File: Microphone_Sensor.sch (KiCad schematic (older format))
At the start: 21 parts

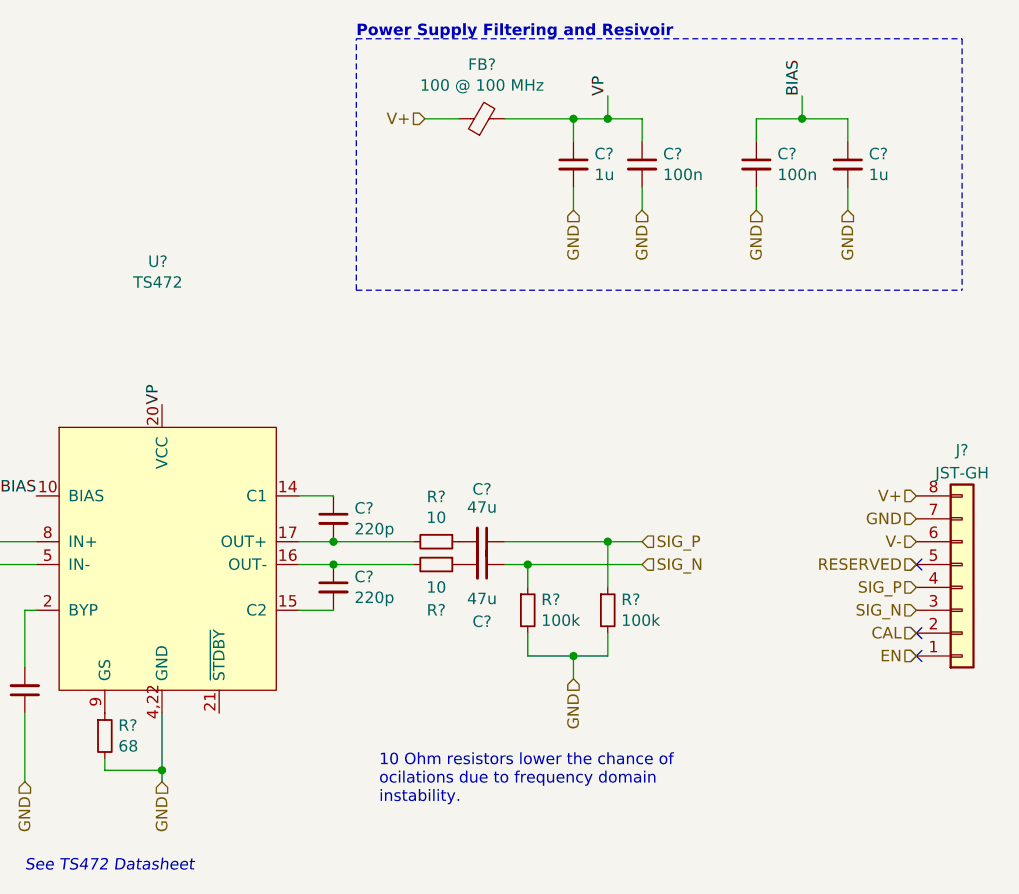
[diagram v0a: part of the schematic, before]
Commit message: Change Connector Layout
Also add Mic. board to connectors
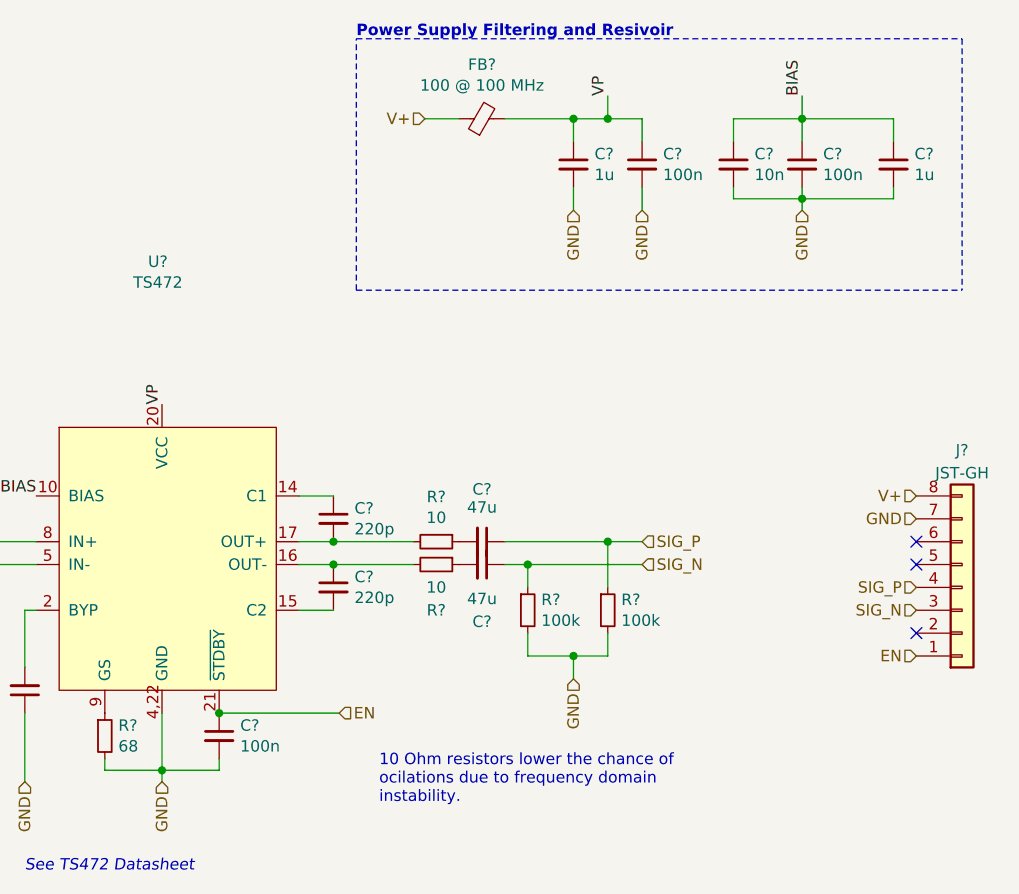
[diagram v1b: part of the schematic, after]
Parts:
- added C?: 100n, symbol Device:C_Small
- added C?: 10n, symbol Device:C_Small
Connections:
- net BIAS: now also C?.1
- net EN: now also U?.21 (~STDBY), C?.1
- net GND: now also C?.2, C?.2
- net CAL: no longer names the net of J?.2 (Pin_2)
- net RESERVED: no longer names the net of J?.5 (Pin_5)
- net V-: no longer names the net of J?.6 (Pin_6)
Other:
- moved on the sheet: C?
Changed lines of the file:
@@
 $Descr A4 11693 8268
 encoding utf-8
-Sheet 14 14
+Sheet 12 14
 Title ""
 Date ""
@@
 U 1 1 5EEDE2AE
 P 4150 2900
+AR Path="/5EE5ECAD/5EECE6B8/5EEDE2AE" Ref="MK?"  Part="1"
+AR Path="/5EE5ECAD/5EF21991/5EEDE2AE" Ref="MK?"  Part="1"
+AR Path="/5EE5ECAD/5EF33EA2/5EEDE2AE" Ref="MK?"  Part="1"
 F 0 "MK?" H 3623 2921 50  0000 R CNN
 F 1 "MIC_ICS_40300" H 3623 2830 50  0000 R CNN
@@
 U 1 1 5EEDEA2B
 P 5150 2900
+AR Path="/5EE5ECAD/5EECE6B8/5EEDEA2B" Ref="C?"  Part="1"
+AR Path="/5EE5ECAD/5EF21991/5EEDEA2B" Ref="C?"  Part="1"
+AR Path="/5EE5ECAD/5EF33EA2/5EEDEA2B" Ref="C?"  Part="1"
 F 0 "C?" V 4921 2900 50  0000 C CNN
 F 1 "1u" V 5000 2900 50  0000 C CNN
@@
 AR Path="/5EE5ECAD/5EE94935/5EEE2D96" Ref="J?"  Part="1"
 AR Path="/5EE1D522/5EEE2D96" Ref="J?"  Part="1"
+AR Path="/5EE5ECAD/5EECE6B8/5EEE2D96" Ref="J?"  Part="1"
+AR Path="/5EE5ECAD/5EF21991/5EEE2D96" Ref="J?"  Part="1"
+AR Path="/5EE5ECAD/5EF33EA2/5EEE2D96" Ref="J?"  Part="1"
 F 0 "J?" H 9950 2500 50  0000 C CNN
 F 1 "JST-GH" H 9950 2600 50  0000 C CNN
@@
 L Device:C_Small C?
 U 1 1 5EEFDD4C
-P 9050 1250
-F 0 "C?" H 9142 1296 50  0000 L CNN
-F 1 "100n" H 9142 1205 50  0000 L CNN
-F 2 "" H 9050 1250 50  0001 C CNN
-F 3 "~" H 9050 1250 50  0001 C CNN
-	1    9050 1250
-	1    0    0    -1
-$EndComp
-Wire Wire Line
-	9050 1050 9050 1150
-Wire Wire Line
-	9050 1350 9050 1450
+P 9250 1250
+AR Path="/5EE5ECAD/5EECE6B8/5EEFDD4C" Ref="C?"  Part="1"
+AR Path="/5EE5ECAD/5EF21991/5EEFDD4C" Ref="C?"  Part="1"
+AR Path="/5EE5ECAD/5EF33EA2/5EEFDD4C" Ref="C?"  Part="1"
+F 0 "C?" H 9342 1296 50  0000 L CNN
+F 1 "100n" H 9342 1205 50  0000 L CNN
+F 2 "" H 9250 1250 50  0001 C CNN
+F 3 "~" H 9250 1250 50  0001 C CNN
+	1    9250 1250
+	1    0    0    -1
+$EndComp
+Wire Wire Line
+	9250 1050 9250 1150
+Wire Wire Line
+	9250 1350 9250 1400
 Text Notes 7300 700  0    50   ~ 10
 Power Supply Filtering and Resivoir
@@
 Text HLabel 9750 2800 0    50   Input ~ 0
 GND
-Text HLabel 9750 2900 0    50   Input ~ 0
-V-
 Text HLabel 9750 3100 0    50   Input ~ 0
 SIG_P
 Text HLabel 9750 3200 0    50   Input ~ 0
 SIG_N
-Text HLabel 9750 3300 0    50   Input ~ 0
-CAL
 Text HLabel 9750 3400 0    50   Input ~ 0
 EN
-Text HLabel 9750 3000 0    50   Input ~ 0
-RESERVED
 NoConn ~ 9750 3000
-NoConn ~ 9750 3400
 NoConn ~ 9750 3300
 $Comp
@@
 U 1 1 5EF35019
 P 7850 1050
+AR Path="/5EE5ECAD/5EECE6B8/5EF35019" Ref="FB?"  Part="1"
+AR Path="/5EE5ECAD/5EF21991/5EF35019" Ref="FB?"  Part="1"
+AR Path="/5EE5ECAD/5EF33EA2/5EF35019" Ref="FB?"  Part="1"
 F 0 "FB?" V 8087 1050 50  0000 C CNN
 F 1 "100 @ 100 MHz" V 7996 1050 50  0000 C CNN
@@
 Text HLabel 7600 1050 0    50   Input ~ 0
 V+
-Text HLabel 9050 1450 3    50   Input ~ 0
+Text HLabel 9250 1450 3    50   Input ~ 0
 GND
 Wire Notes Line
@@
 U 1 1 5EE1252E
 P 6450 2950
+AR Path="/5EE5ECAD/5EECE6B8/5EE1252E" Ref="U?"  Part="1"
+AR Path="/5EE5ECAD/5EF21991/5EE1252E" Ref="U?"  Part="1"
+AR Path="/5EE5ECAD/5EF33EA2/5EE1252E" Ref="U?"  Part="1"
 F 0 "U?" H 6432 4225 50  0000 C CNN
 F 1 "TS472" H 6432 4134 50  0000 C CNN
@@
 U 1 1 5EE150A7
 P 4950 3000
+AR Path="/5EE5ECAD/5EECE6B8/5EE150A7" Ref="R?"  Part="1"
+AR Path="/5EE5ECAD/5EF21991/5EE150A7" Ref="R?"  Part="1"
+AR Path="/5EE5ECAD/5EF33EA2/5EE150A7" Ref="R?"  Part="1"
 F 0 "R?" V 5150 3000 50  0000 C CNN
 F 1 "220" V 5050 3000 50  0000 C CNN
@@
 U 1 1 5EE19951
 P 5150 3000
+AR Path="/5EE5ECAD/5EECE6B8/5EE19951" Ref="C?"  Part="1"
+AR Path="/5EE5ECAD/5EF21991/5EE19951" Ref="C?"  Part="1"
+AR Path="/5EE5ECAD/5EF33EA2/5EE19951" Ref="C?"  Part="1"
 F 0 "C?" V 5400 3000 50  0000 C CNN
 F 1 "1u" V 5300 3000 50  0000 C CNN
@@
 U 1 1 5EE1EACE
 P 5850 3550
+AR Path="/5EE5ECAD/5EECE6B8/5EE1EACE" Ref="C?"  Part="1"
+AR Path="/5EE5ECAD/5EF21991/5EE1EACE" Ref="C?"  Part="1"
+AR Path="/5EE5ECAD/5EF33EA2/5EE1EACE" Ref="C?"  Part="1"
 F 0 "C?" V 6100 3550 50  0000 C CNN
 F 1 "1u" V 6000 3550 50  0000 C CNN
@@
 U 1 1 5EE21893
 P 6200 3750
+AR Path="/5EE5ECAD/5EECE6B8/5EE21893" Ref="R?"  Part="1"
+AR Path="/5EE5ECAD/5EF21991/5EE21893" Ref="R?"  Part="1"
+AR Path="/5EE5ECAD/5EF33EA2/5EE21893" Ref="R?"  Part="1"
 F 0 "R?" H 6259 3796 50  0000 L CNN
 F 1 "68" H 6259 3705 50  0000 L CNN
@@
 U 1 1 5EE3D7C0
 P 8250 1250
+AR Path="/5EE5ECAD/5EECE6B8/5EE3D7C0" Ref="C?"  Part="1"
+AR Path="/5EE5ECAD/5EF21991/5EE3D7C0" Ref="C?"  Part="1"
+AR Path="/5EE5ECAD/5EF33EA2/5EE3D7C0" Ref="C?"  Part="1"
 F 0 "C?" H 8342 1296 50  0000 L CNN
 F 1 "1u" H 8342 1205 50  0000 L CNN
@@
 L Device:C_Small C?
 U 1 1 5EE4D182
-P 9450 1250
-F 0 "C?" H 9542 1296 50  0000 L CNN
-F 1 "1u" H 9542 1205 50  0000 L CNN
-F 2 "" H 9450 1250 50  0001 C CNN
-F 3 "~" H 9450 1250 50  0001 C CNN
-	1    9450 1250
-	1    0    0    -1
-$EndComp
-Wire Wire Line
-	9450 1050 9450 1150
-Wire Wire Line
-	9450 1350 9450 1450
-Text HLabel 9450 1450 3    50   Input ~ 0
-GND
+P 9650 1250
+AR Path="/5EE5ECAD/5EECE6B8/5EE4D182" Ref="C?"  Part="1"
+AR Path="/5EE5ECAD/5EF21991/5EE4D182" Ref="C?"  Part="1"
+AR Path="/5EE5ECAD/5EF33EA2/5EE4D182" Ref="C?"  Part="1"
+F 0 "C?" H 9742 1296 50  0000 L CNN
+F 1 "1u" H 9742 1205 50  0000 L CNN
+F 2 "" H 9650 1250 50  0001 C CNN
+F 3 "~" H 9650 1250 50  0001 C CNN
+	1    9650 1250
+	1    0    0    -1
+$EndComp
+Wire Wire Line
+	9650 1050 9650 1150
+Wire Wire Line
+	9650 1350 9650 1400
 Text Label 9250 950  1    50   ~ 0
 BIAS
@@
 U 1 1 5EE3C381
 P 8550 1250
+AR Path="/5EE5ECAD/5EECE6B8/5EE3C381" Ref="C?"  Part="1"
+AR Path="/5EE5ECAD/5EF21991/5EE3C381" Ref="C?"  Part="1"
+AR Path="/5EE5ECAD/5EF33EA2/5EE3C381" Ref="C?"  Part="1"
 F 0 "C?" H 8642 1296 50  0000 L CNN
 F 1 "100n" H 8642 1205 50  0000 L CNN
@@
 $EndComp
 Wire Wire Line
-	9450 1050 9250 1050
+	9650 1050 9250 1050
 Wire Wire Line
 	9250 950  9250 1050
 Connection ~ 9250 1050
-Wire Wire Line
-	9250 1050 9050 1050
 $Comp
 L Device:C_Small C?
 U 1 1 5EE64CD6
 P 7200 3100
+AR Path="/5EE5ECAD/5EECE6B8/5EE64CD6" Ref="C?"  Part="1"
+AR Path="/5EE5ECAD/5EF21991/5EE64CD6" Ref="C?"  Part="1"
+AR Path="/5EE5ECAD/5EF33EA2/5EE64CD6" Ref="C?"  Part="1"
 F 0 "C?" H 7292 3146 50  0000 L CNN
 F 1 "220p" H 7292 3055 50  0000 L CNN
@@
 U 1 1 5EE65504
 P 7200 2800
+AR Path="/5EE5ECAD/5EECE6B8/5EE65504" Ref="C?"  Part="1"
+AR Path="/5EE5ECAD/5EF21991/5EE65504" Ref="C?"  Part="1"
+AR Path="/5EE5ECAD/5EF33EA2/5EE65504" Ref="C?"  Part="1"
 F 0 "C?" H 7292 2846 50  0000 L CNN
 F 1 "220p" H 7292 2755 50  0000 L CNN
@@
 U 1 1 5EE68FFE
 P 8050 3200
+AR Path="/5EE5ECAD/5EECE6B8/5EE68FFE" Ref="R?"  Part="1"
+AR Path="/5EE5ECAD/5EF21991/5EE68FFE" Ref="R?"  Part="1"
+AR Path="/5EE5ECAD/5EF33EA2/5EE68FFE" Ref="R?"  Part="1"
 F 0 "R?" H 8109 3246 50  0000 L CNN
 F 1 "100k" H 8109 3155 50  0000 L CNN
@@
 U 1 1 5EE699A6
 P 8400 3200
+AR Path="/5EE5ECAD/5EECE6B8/5EE699A6" Ref="R?"  Part="1"
+AR Path="/5EE5ECAD/5EF21991/5EE699A6" Ref="R?"  Part="1"
+AR Path="/5EE5ECAD/5EF33EA2/5EE699A6" Ref="R?"  Part="1"
 F 0 "R?" H 8459 3246 50  0000 L CNN
 F 1 "100k" H 8459 3155 50  0000 L CNN
@@
 U 1 1 5EE840BE
 P 7650 2900
+AR Path="/5EE5ECAD/5EECE6B8/5EE840BE" Ref="R?"  Part="1"
+AR Path="/5EE5ECAD/5EF21991/5EE840BE" Ref="R?"  Part="1"
+AR Path="/5EE5ECAD/5EF33EA2/5EE840BE" Ref="R?"  Part="1"
 F 0 "R?" V 7454 2900 50  0000 C CNN
 F 1 "10" V 7545 2900 50  0000 C CNN
@@
 U 1 1 5EE845A7
 P 7650 3000
+AR Path="/5EE5ECAD/5EECE6B8/5EE845A7" Ref="R?"  Part="1"
+AR Path="/5EE5ECAD/5EF21991/5EE845A7" Ref="R?"  Part="1"
+AR Path="/5EE5ECAD/5EF33EA2/5EE845A7" Ref="R?"  Part="1"
 F 0 "R?" V 7850 3000 50  0000 C CNN
 F 1 "10" V 7750 3000 50  0000 C CNN
@@
 U 1 1 5EE94347
 P 7850 2900
+AR Path="/5EE5ECAD/5EECE6B8/5EE94347" Ref="C?"  Part="1"
+AR Path="/5EE5ECAD/5EF21991/5EE94347" Ref="C?"  Part="1"
+AR Path="/5EE5ECAD/5EF33EA2/5EE94347" Ref="C?"  Part="1"
 F 0 "C?" V 7621 2900 50  0000 C CNN
 F 1 "47u" V 7700 2900 50  0000 C CNN
@@
 U 1 1 5EE9434D
 P 7850 3000
+AR Path="/5EE5ECAD/5EECE6B8/5EE9434D" Ref="C?"  Part="1"
+AR Path="/5EE5ECAD/5EF21991/5EE9434D" Ref="C?"  Part="1"
+AR Path="/5EE5ECAD/5EF33EA2/5EE9434D" Ref="C?"  Part="1"
 F 0 "C?" V 8100 3000 50  0000 C CNN
 F 1 "47u" V 8000 3000 50  0000 C CNN
@@
 	0    1    1    0
 $EndComp
+NoConn ~ 9750 2900
+Text HLabel 7225 3650 2    50   Input ~ 0
+EN
+$Comp
+L Device:C_Small C?
+U 1 1 5EEDB218
+P 6700 3750
+AR Path="/5EE5ECAD/5EECE6B8/5EEDB218" Ref="C?"  Part="1"
+AR Path="/5EE5ECAD/5EF21991/5EEDB218" Ref="C?"  Part="1"
+AR Path="/5EE5ECAD/5EF33EA2/5EEDB218" Ref="C?"  Part="1"
+F 0 "C?" H 6792 3796 50  0000 L CNN
+F 1 "100n" H 6792 3705 50  0000 L CNN
+F 2 "" H 6700 3750 50  0001 C CNN
+F 3 "~" H 6700 3750 50  0001 C CNN
+	1    6700 3750
+	1    0    0    -1
+$EndComp
+$Comp
+L Device:C_Small C?
+U 1 1 5EEE5C9C
+P 8950 1250
+AR Path="/5EE5ECAD/5EECE6B8/5EEE5C9C" Ref="C?"  Part="1"
+AR Path="/5EE5ECAD/5EF21991/5EEE5C9C" Ref="C?"  Part="1"
+AR Path="/5EE5ECAD/5EF33EA2/5EEE5C9C" Ref="C?"  Part="1"
+F 0 "C?" H 9042 1296 50  0000 L CNN
+F 1 "10n" H 9042 1205 50  0000 L CNN
+F 2 "" H 8950 1250 50  0001 C CNN
+F 3 "~" H 8950 1250 50  0001 C CNN
+	1    8950 1250
+	1    0    0    -1
+$EndComp
+Wire Wire Line
+	8950 1150 8950 1050
+Wire Wire Line
+	8950 1050 9250 1050
+Wire Wire Line
+	8950 1350 8950 1400
+Wire Wire Line
+	8950 1400 9250 1400
+Connection ~ 9250 1400
+Wire Wire Line
+	9250 1400 9250 1450
+Wire Wire Line
+	9250 1400 9650 1400
+Wire Wire Line
+	6700 3850 6700 3900
+Wire Wire Line
+	6700 3900 6450 3900
+Wire Wire Line
+	7225 3650 6700 3650
+Connection ~ 6700 3650
 $EndSCHEMATC

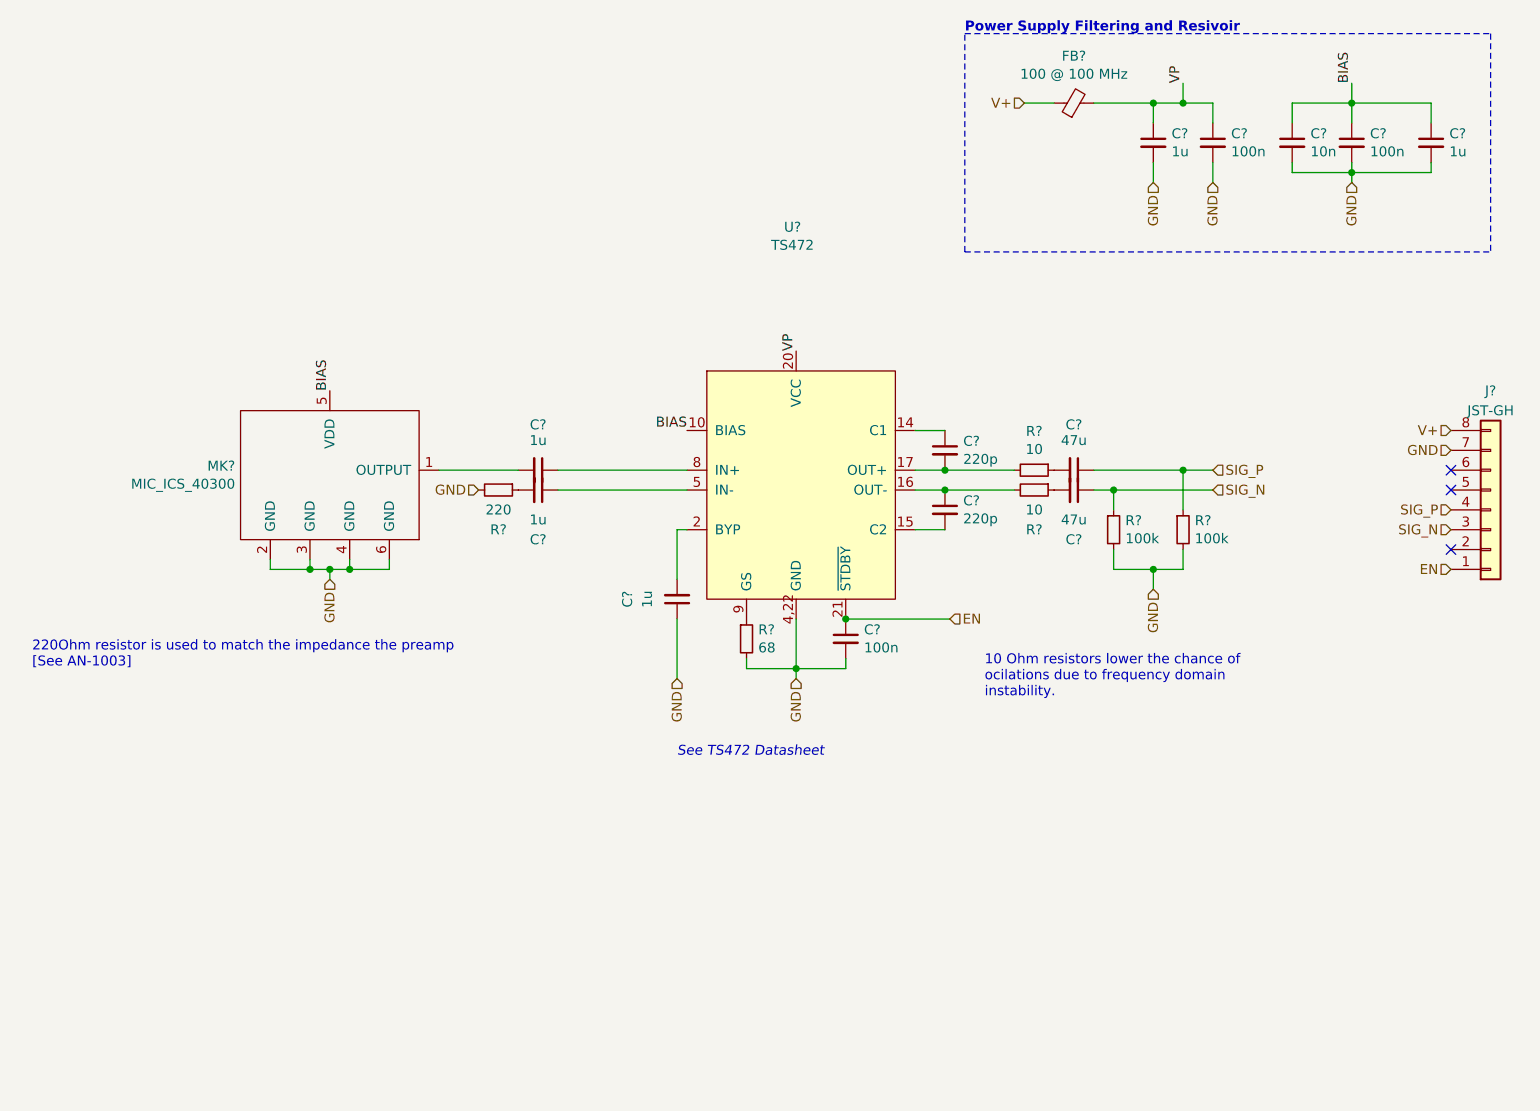
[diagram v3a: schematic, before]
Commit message: Add PWR Flags
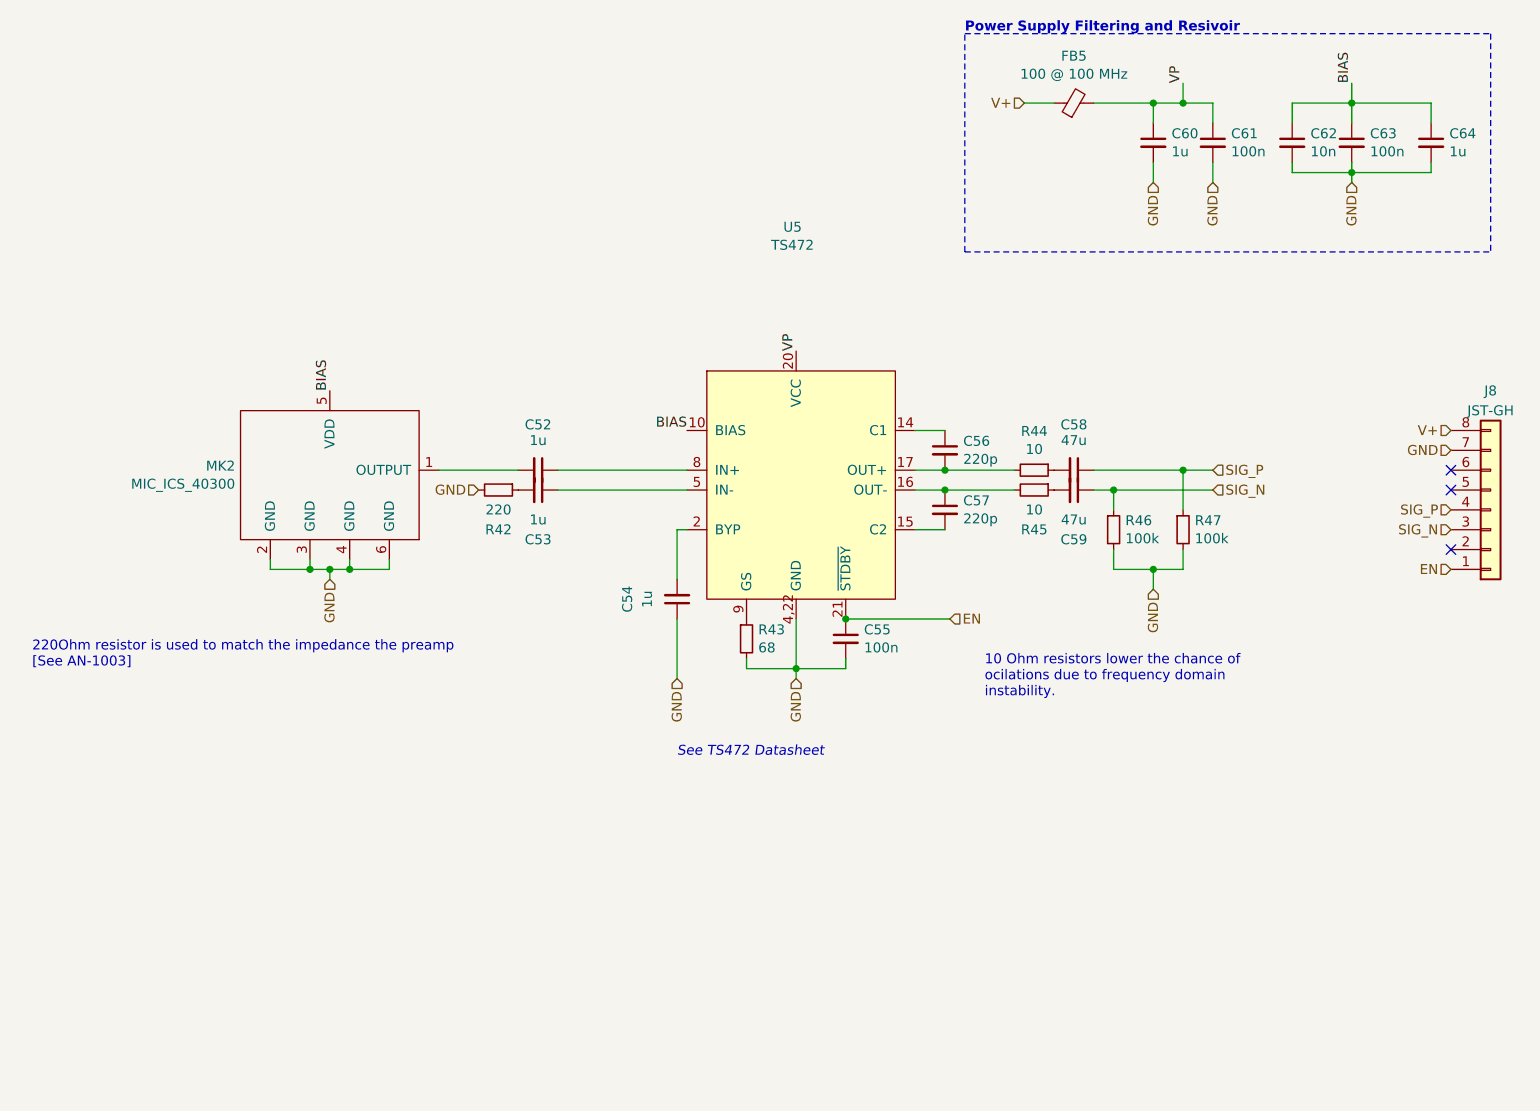
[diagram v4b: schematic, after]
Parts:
- gave numbers to parts that had none: 23
